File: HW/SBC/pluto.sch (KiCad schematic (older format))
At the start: 0 parts

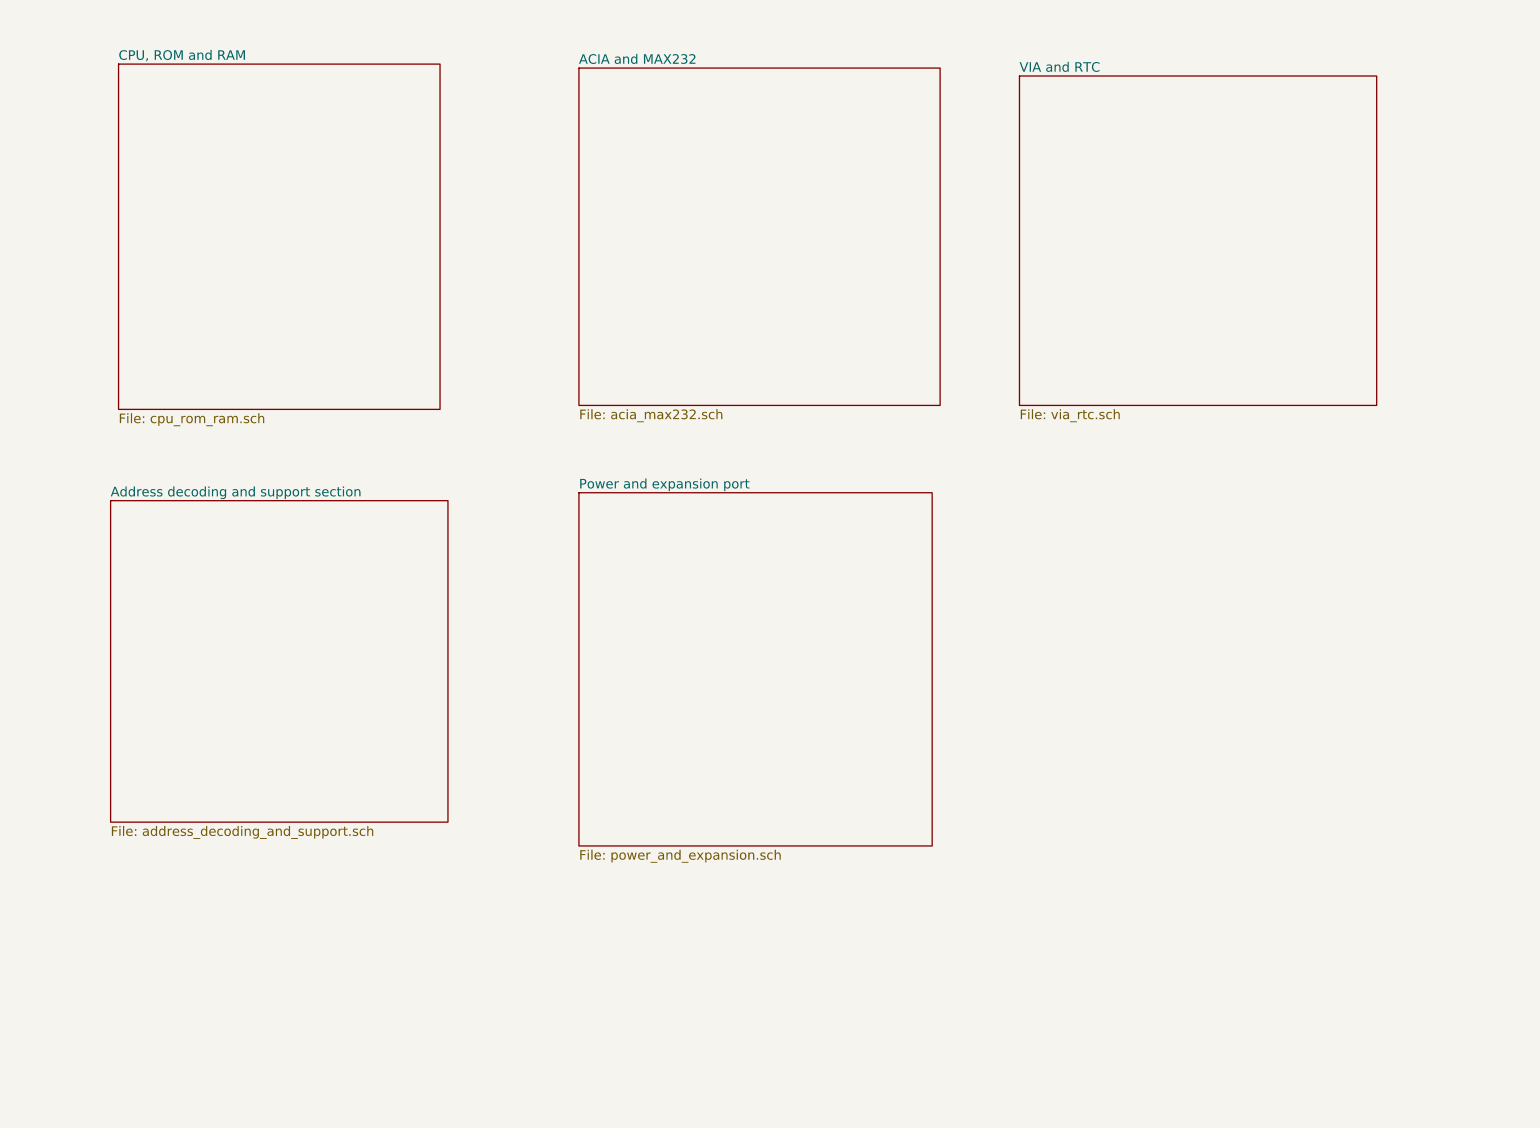
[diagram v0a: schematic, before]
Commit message: New schema. Adding a VIA and sound chip.
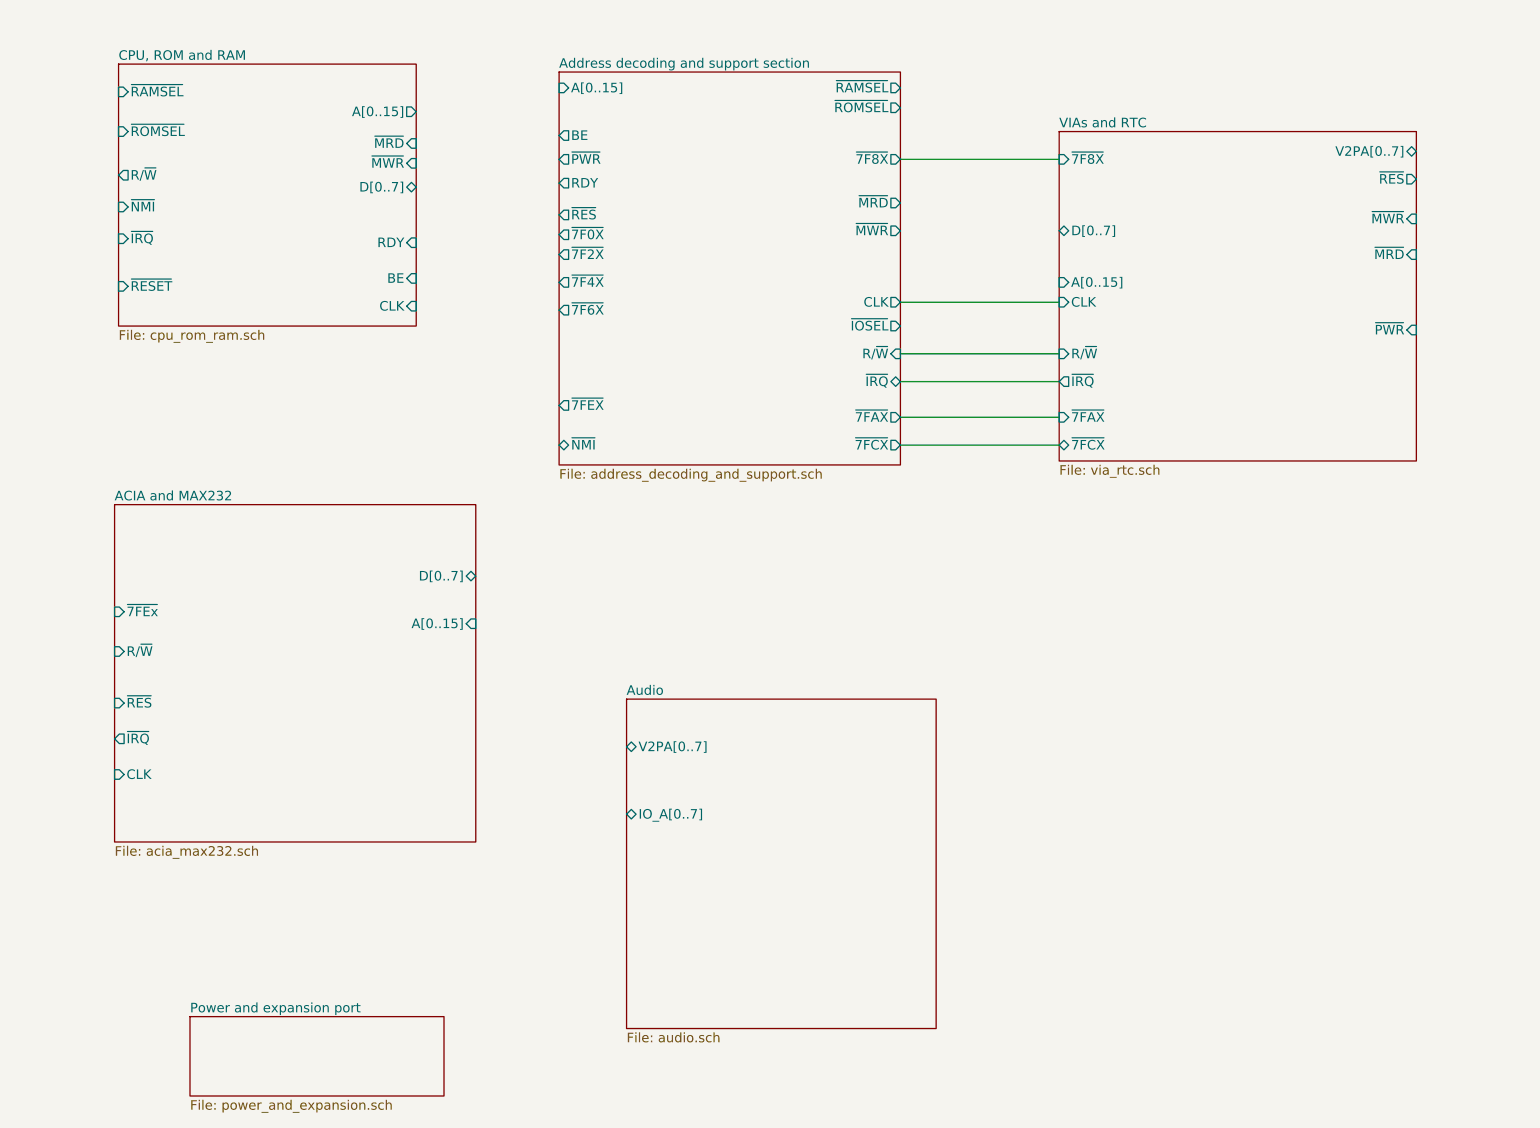
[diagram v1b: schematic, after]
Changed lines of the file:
@@
 LIBS:zetex
 LIBS:Zilog
+LIBS:pluto
 LIBS:pluto-cache
 EELAYER 25 0
@@
 $Descr A4 11693 8268
 encoding utf-8
-Sheet 1 6
+Sheet 1 7
 Title "Pluto SCB"
 Date "2017-03-25"
@@
 $EndDescr
 $Sheet
-S 1400 900  2025 2175
+S 1400 900  1875 1650
 U 58D5892B
 F0 "CPU, ROM and RAM" 60
 F1 "cpu_rom_ram.sch" 60
+F2 "A[0..15]" O R 3275 1200 60
+F3 "D[0..7]" B R 3275 1675 60
+F4 "RDY" I R 3275 2025 60
+F5 "BE" I R 3275 2250 60
+F6 "~IRQ" I L 1400 2000 60
+F7 "R/~W" O L 1400 1600 60
+F8 "~NMI" I L 1400 1800 60
+F9 "~RESET" I L 1400 2300 60
+F10 "CLK" I R 3275 2425 60
+F11 "~MRD" I R 3275 1400 60
+F12 "~MWR" I R 3275 1525 60
+F13 "~RAMSEL" I L 1400 1075 60
+F14 "~ROMSEL" I L 1400 1325 60
 $EndSheet
 $Sheet
-S 4300 925  2275 2125
+S 1375 3675 2275 2125
 U 58D58957
 F0 "ACIA and MAX232" 60
 F1 "acia_max232.sch" 60
+F2 "~7FEx" I L 1375 4350 60
+F3 "R/~W" I L 1375 4600 60
+F4 "~RES" I L 1375 4925 60
+F5 "~IRQ" O L 1375 5150 60
+F6 "CLK" I L 1375 5375 60
+F7 "D[0..7]" B R 3650 4125 60
+F8 "A[0..15]" I R 3650 4425 60
 $EndSheet
 $Sheet
-S 7075 975  2250 2075
+S 7325 1325 2250 2075
 U 58D58980
-F0 "VIA and RTC" 60
+F0 "VIAs and RTC" 60
 F1 "via_rtc.sch" 60
+F2 "V2PA[0..7]" B R 9575 1450 60
+F3 "D[0..7]" B L 7325 1950 60
+F4 "~7FCX" B L 7325 3300 60
+F5 "A[0..15]" I L 7325 2275 60
+F6 "~PWR" I R 9575 2575 60
+F7 "~RES" O R 9575 1625 60
+F8 "~IRQ" O L 7325 2900 60
+F9 "~MWR" I R 9575 1875 60
+F10 "~MRD" I R 9575 2100 60
+F11 "~7F8X" I L 7325 1500 60
+F12 "~7FAX" I L 7325 3125 60
+F13 "R/~W" I L 7325 2725 60
+F14 "CLK" I L 7325 2400 60
 $EndSheet
 $Sheet
-S 1350 3650 2125 2025
+S 4175 950  2150 2475
 U 58D589A4
 F0 "Address decoding and support section" 60
 F1 "address_decoding_and_support.sch" 60
+F2 "CLK" O R 6325 2400 60
+F3 "A[0..15]" I L 4175 1050 60
+F4 "~MRD" O R 6325 1775 60
+F5 "~MWR" O R 6325 1950 60
+F6 "~ROMSEL" O R 6325 1175 60
+F7 "~RAMSEL" O R 6325 1050 60
+F8 "~IOSEL" O R 6325 2550 60
+F9 "R/~W" I R 6325 2725 60
+F10 "~IRQ" B R 6325 2900 60
+F11 "~NMI" B L 4175 3300 60
+F12 "BE" O L 4175 1350 60
+F13 "~PWR" O L 4175 1500 60
+F14 "RDY" O L 4175 1650 60
+F15 "~RES" O L 4175 1850 60
+F16 "~7F0X" O L 4175 1975 60
+F17 "~7F2X" O L 4175 2100 60
+F18 "~7F4X" O L 4175 2275 60
+F19 "~7F6X" O L 4175 2450 60
+F20 "~7F8X" O R 6325 1500 60
+F21 "~7FAX" O R 6325 3125 60
+F22 "~7FCX" O R 6325 3300 60
+F23 "~7FEX" O L 4175 3050 60
 $EndSheet
 $Sheet
-S 4300 3600 2225 2225
+S 1850 6900 1600 500
 U 58D589DC
 F0 "Power and expansion port" 60
 F1 "power_and_expansion.sch" 60
 $EndSheet
+$Sheet
+S 4600 4900 1950 2075
+U 59306E56
+F0 "Audio" 60
+F1 "audio.sch" 60
+F2 "V2PA[0..7]" B L 4600 5200 60
+F3 "IO_A[0..7]" B L 4600 5625 60
+$EndSheet
+Wire Wire Line
+	6325 3125 7325 3125
+Wire Wire Line
+	6325 3300 7325 3300
+Wire Wire Line
+	6325 2900 7325 2900
+Wire Wire Line
+	6325 2725 7325 2725
+Wire Wire Line
+	6325 2400 7325 2400
+Wire Wire Line
+	6325 1500 7325 1500
 $EndSCHEMATC

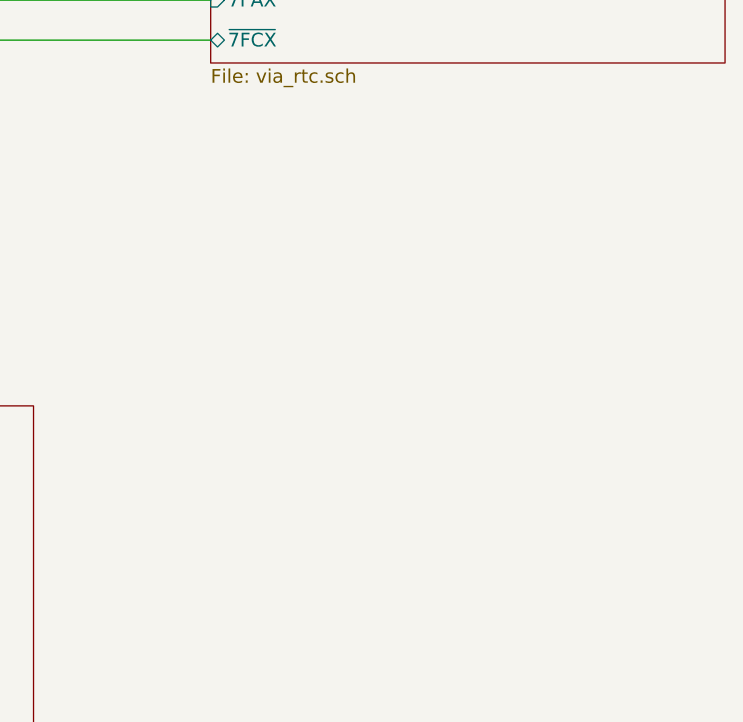
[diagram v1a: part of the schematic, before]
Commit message: Moved IDE schematics (WIP) into pluto.
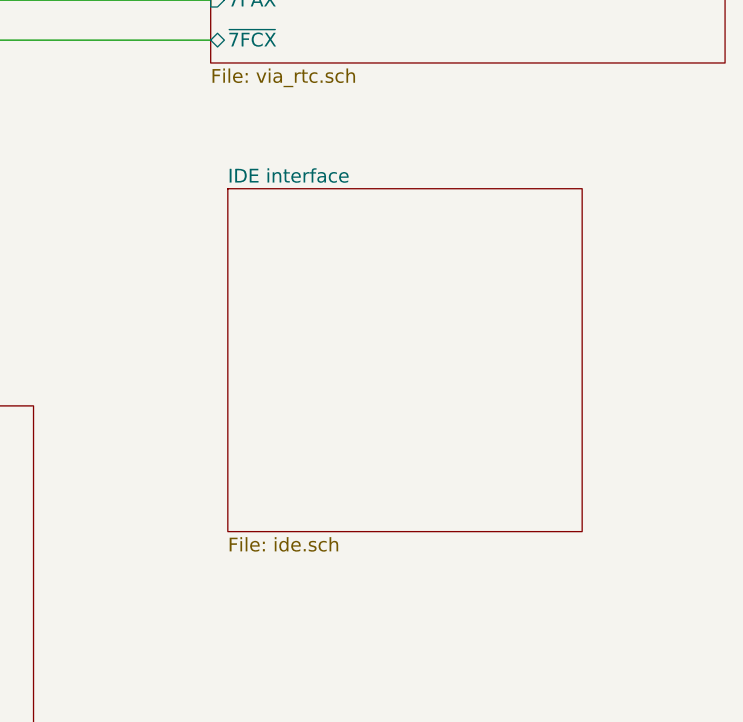
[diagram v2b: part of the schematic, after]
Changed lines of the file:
@@
 EESchema Schematic File Version 2
+LIBS:pluto-rescue
 LIBS:power
 LIBS:device
@@
 $Descr A4 11693 8268
 encoding utf-8
-Sheet 1 7
+Sheet 1 8
 Title "Pluto SCB"
 Date "2017-03-25"
@@
 Wire Wire Line
 	6325 1500 7325 1500
+$Sheet
+S 7400 3950 1550 1500
+U 5932E4CB
+F0 "IDE interface" 60
+F1 "ide.sch" 60
+$EndSheet
 $EndSCHEMATC

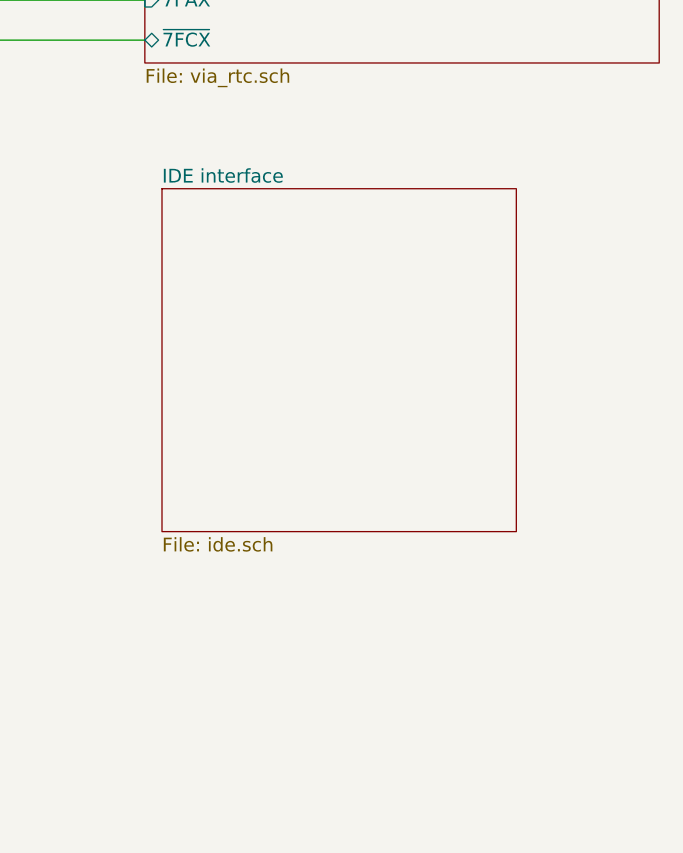
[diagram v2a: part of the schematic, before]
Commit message: Added IDE interface to PLUTO board.
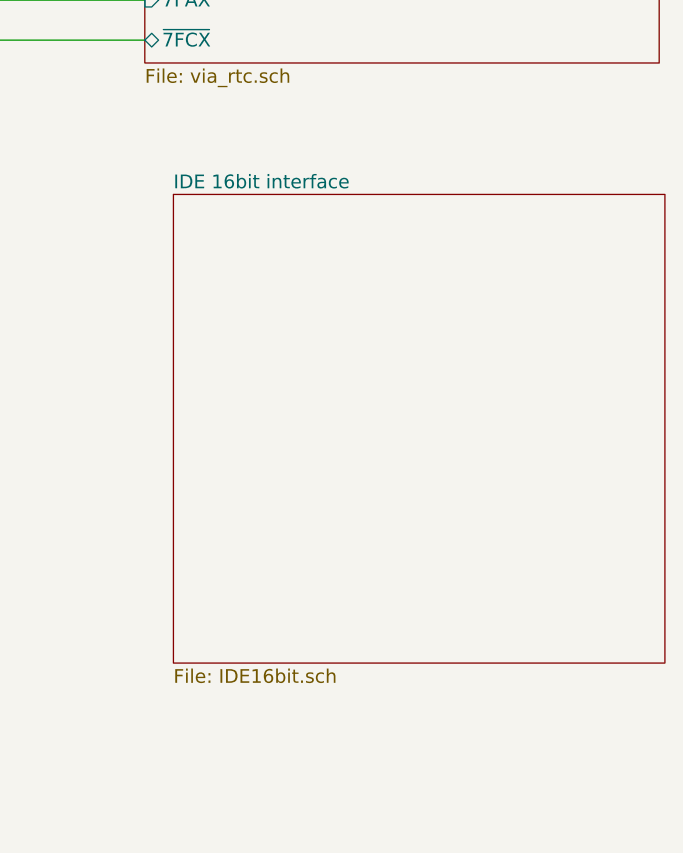
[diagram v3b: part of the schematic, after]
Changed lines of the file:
@@
 LIBS:pluto
 LIBS:pluto-cache
+LIBS:IDE_interface-cache
 EELAYER 25 0
 EELAYER END
@@
 	6325 1500 7325 1500
 $Sheet
-S 7400 3950 1550 1500
-U 5932E4CB
-F0 "IDE interface" 60
-F1 "ide.sch" 60
+S 7450 3975 2150 2050
+U 5932EBB3
+F0 "IDE 16bit interface" 60
+F1 "IDE16bit.sch" 60
 $EndSheet
 $EndSCHEMATC

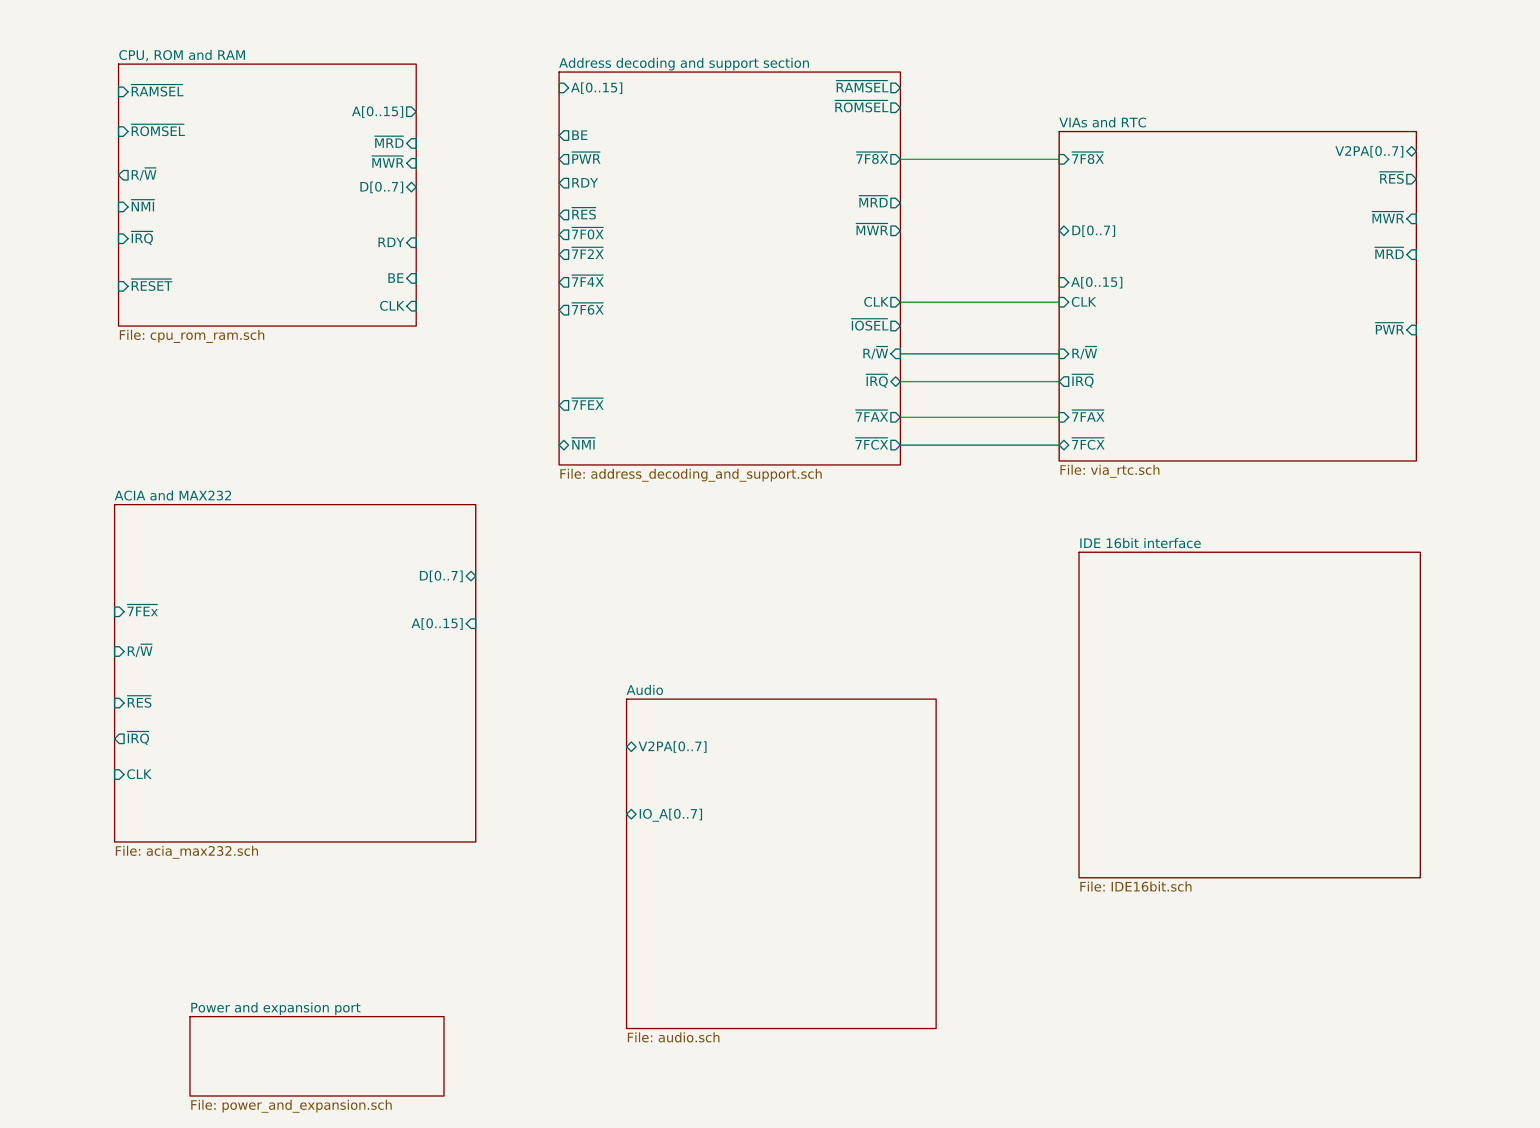
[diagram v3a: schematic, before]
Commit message: Connected most hierarchical labels between the sheets. Added a connector to AY IO port.
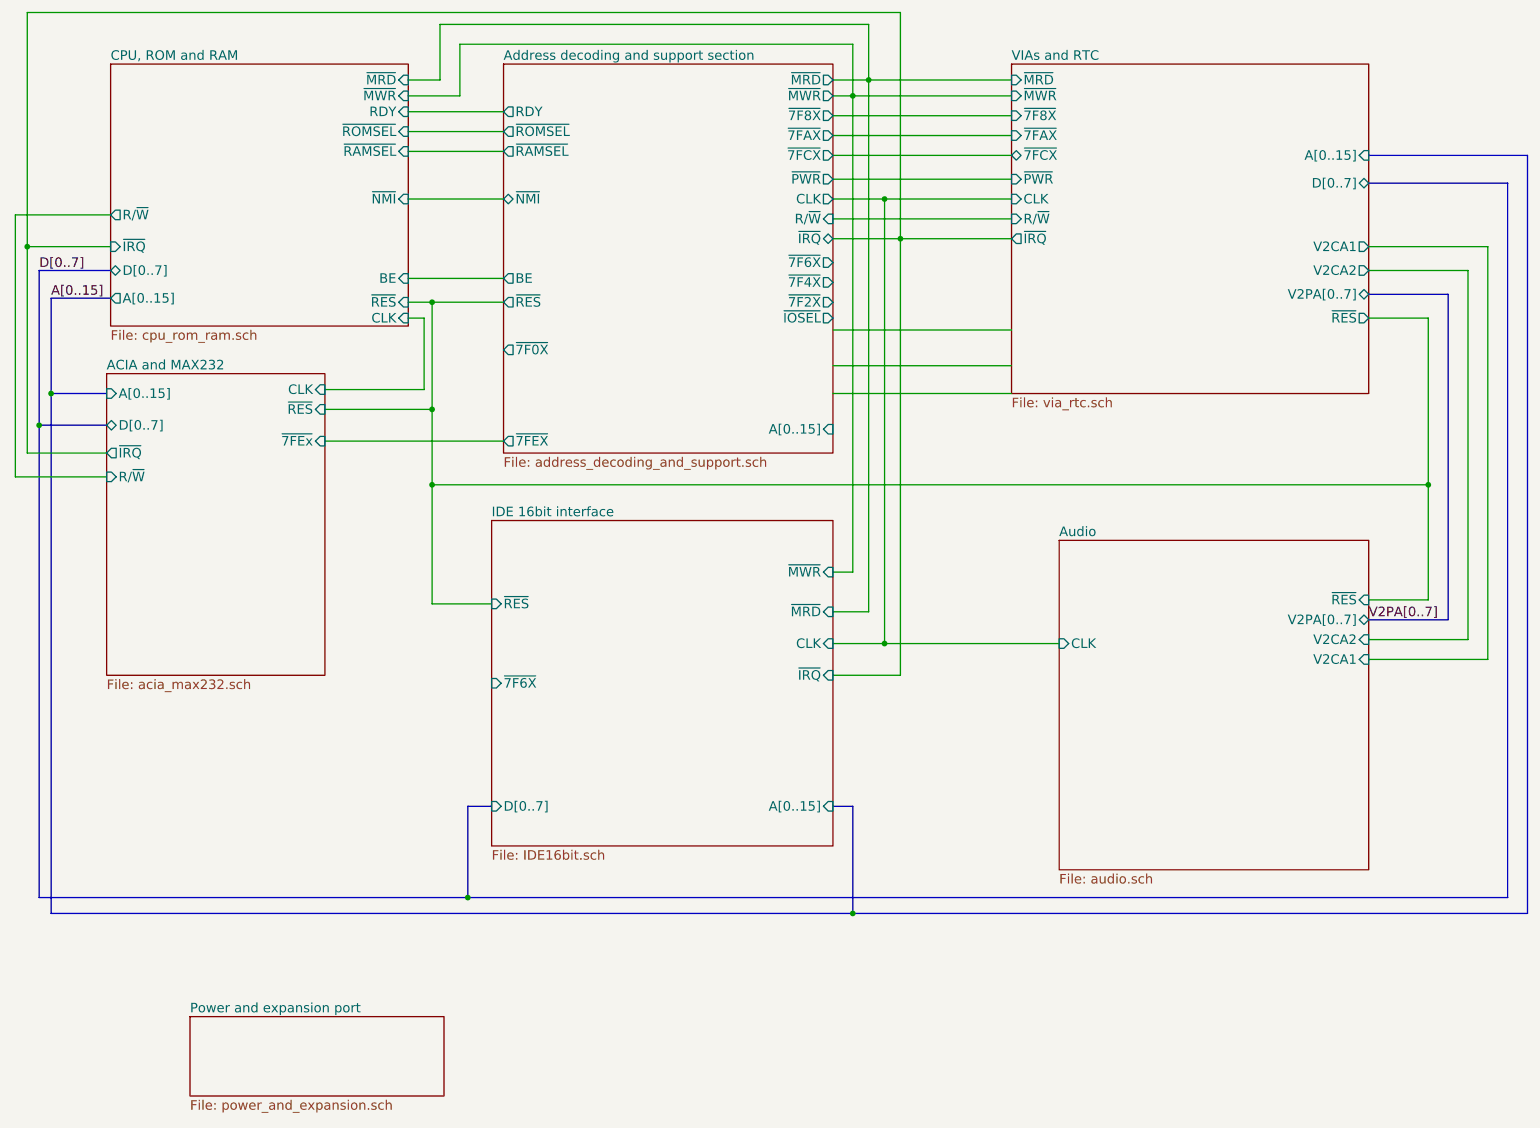
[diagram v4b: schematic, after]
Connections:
- net labels added: A[0..15], D[0..7], V2PA[0..7]
- wire segments 6 -> 56
